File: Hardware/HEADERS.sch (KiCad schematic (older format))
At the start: 47 parts, among them J16 SPOX-3, J17 SPOX-3, J18 SPOX-4, J19 SPOX-2, J20 SPOX-3, J22 SPOX-4, J23 SPOX-4, J24 SPOX-6, J25 SPOX-6, J26 SPOX-6, J28 SPOX-6, J29 SPOX-6, J30 SPOX-6

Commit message: Add files via upload
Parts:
- removed TP19: GPIOL0_1_TST, Measurement_Points:Measurement_Point_Round-SMD-Pad_Small, symbol TEST
- removed TP22: GPIOL0_2_TST, Measurement_Points:Measurement_Point_Round-SMD-Pad_Small, symbol TEST
- removed TP30, TP31, TP32, TP33, TP34, TP35: TEST, Measurement_Points:Measurement_Point_Round-SMD-Pad_Small, symbol TEST
- added J21: SPOX-4, Connectors_Molex:Molex_SPOX-5267_22-03-5045_04x2.54mm_Straight, symbol SPOX-4
- added J27: SPOX-6, Connectors_Molex:Molex_SPOX-5267_22-03-5065_06x2.54mm_Straight, symbol SPOX-6
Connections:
- net GND: now also J21.1, J27.1
- net SCL1: now also J21.3
- net SDA1: now also J21.4
- net SPI1_CK: now also J27.5
- net SPI1_SDO: now also J27.4
- net SPI1_SI: now also J27.3
- net SPI1_SS: now also J27.2
- net V_I2C: now also J21.2
- net V_SPI: now also J27.6
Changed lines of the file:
@@
 DBG_TX_SAFETY
 $Comp
-L GND #PWR60
+L GND #PWR060
 U 1 1 5923E07E
 P 4050 5300
-F 0 "#PWR60" H 4050 5050 50  0001 C CNN
+F 0 "#PWR060" H 4050 5050 50  0001 C CNN
 F 1 "GND" H 4050 5150 50  0000 C CNN
 F 2 "" H 4050 5300 50  0001 C CNN
@@
 SCL4
 $Comp
-L GND #PWR61
+L GND #PWR061
 U 1 1 5923E229
 P 6500 5700
-F 0 "#PWR61" H 6500 5450 50  0001 C CNN
+F 0 "#PWR061" H 6500 5450 50  0001 C CNN
 F 1 "GND" H 6500 5550 50  0000 C CNN
 F 2 "" H 6500 5700 50  0001 C CNN
@@
 SPI5_CK
 $Comp
-L GND #PWR62
+L GND #PWR062
 U 1 1 5923EE9C
 P 9950 5850
-F 0 "#PWR62" H 9950 5600 50  0001 C CNN
+F 0 "#PWR062" H 9950 5600 50  0001 C CNN
 F 1 "GND" H 9950 5700 50  0000 C CNN
 F 2 "" H 9950 5850 50  0001 C CNN
@@
 $EndComp
 $Comp
-L GND #PWR58
+L GND #PWR063
 U 1 1 5923F1BC
 P 1600 5000
-F 0 "#PWR58" H 1600 4750 50  0001 C CNN
+F 0 "#PWR063" H 1600 4750 50  0001 C CNN
 F 1 "GND" H 1600 4850 50  0000 C CNN
 F 2 "" H 1600 5000 50  0001 C CNN
@@
 UHF_RX
 $Comp
-L GND #PWR59
+L GND #PWR064
 U 1 1 594AA8BD
 P 1900 7000
-F 0 "#PWR59" H 1900 6750 50  0001 C CNN
+F 0 "#PWR064" H 1900 6750 50  0001 C CNN
 F 1 "GND" H 1900 6850 50  0000 C CNN
 F 2 "" H 1900 7000 50  0001 C CNN
@@
 $EndComp
 $Comp
+L SPOX-6 J27
+U 1 1 595BDD44
+P 9000 2900
+F 0 "J27" H 9100 3250 60  0000 C CNN
+F 1 "SPOX-6" H 9100 2550 60  0000 C CNN
+F 2 "Connectors_Molex:Molex_SPOX-5267_22-03-5065_06x2.54mm_Straight" H 9000 3050 60  0001 C CNN
+F 3 "" H 9000 3050 60  0001 C CNN
+F 4 "CONN-005" H 9200 3350 60  0001 C CNN "part_num"
+	1    9000 2900
+	1    0    0    -1
+$EndComp
+$Comp
 L SPOX-6 J28
 U 1 1 595BDD92
@@
 $EndComp
 $Comp
+L SPOX-4 J21
+U 1 1 595C301B
+P 3700 3850
+F 0 "J21" H 3800 4100 60  0000 C CNN
+F 1 "SPOX-4" H 3800 3600 60  0000 C CNN
+F 2 "Connectors_Molex:Molex_SPOX-5267_22-03-5045_04x2.54mm_Straight" H 3700 3900 60  0001 C CNN
+F 3 "" H 3700 3900 60  0001 C CNN
+F 4 "CONN-003" H 3900 4200 60  0001 C CNN "part_num"
+	1    3700 3850
+	1    0    0    -1
+$EndComp
+$Comp
 L SPOX-4 J22
 U 1 1 595C306F
@@
 	1750 3800 1500 3800
 Wire Wire Line
-	4050 4600 4050 5300
+	3900 4000 4050 4000
+Wire Wire Line
+	4050 4000 4050 5300
 Wire Wire Line
 	4050 5150 3900 5150
 Wire Wire Line
 	3900 4600 4050 4600
+Connection ~ 4050 4600
 Connection ~ 4050 5150
 Wire Wire Line
@@
 	3900 4500 4200 4500
 Connection ~ 4200 4500
+Connection ~ 4200 3900
 Wire Wire Line
 	3900 3700 4500 3700
@@
 Wire Wire Line
 	3900 4950 4500 4950
+Wire Wire Line
+	3900 3900 4200 3900
 Wire Wire Line
 	5600 2900 6500 2900
@@
 	9300 3050 9200 3050
 Wire Wire Line
-	9850 2650 10100 2650
+	9200 2650 10100 2650
 Wire Wire Line
 	10100 3500 10100 4300
 Wire Wire Line
-	9950 4000 9950 5850
+	9200 3150 9950 3150
+Wire Wire Line
+	9950 3150 9950 5850
 Wire Wire Line
 	9850 2550 9850 2650
+Connection ~ 9850 2650
 Connection ~ 10100 3500
 Connection ~ 10100 4300
@@
 Wire Wire Line
 	9200 4000 9950 4000
+Connection ~ 9950 4000
 Wire Wire Line
 	3350 3500 3350 3600
@@
 $EndComp
 $Comp
-L TEST TP19
-U 1 1 5B2C6951
-P 3550 6150
-F 0 "TP19" V 3600 7000 50  0000 C BNN
-F 1 "GPIOL0_1_TST" V 3550 6650 50  0000 C CNN
-F 2 "Measurement_Points:Measurement_Point_Round-SMD-Pad_Small" H 3550 6150 50  0001 C CNN
-F 3 "" H 3550 6150 50  0001 C CNN
-	1    3550 6150
-	0    -1   -1   0
-$EndComp
-$Comp
 L TEST TP20
 U 1 1 5B2C6D6F
@@
 $EndComp
 $Comp
-L TEST TP22
-U 1 1 5B2C6D7B
-P 3550 6600
-F 0 "TP22" V 3600 7450 50  0000 C BNN
-F 1 "GPIOL0_2_TST" V 3550 7100 50  0000 C CNN
-F 2 "Measurement_Points:Measurement_Point_Round-SMD-Pad_Small" H 3550 6600 50  0001 C CNN
-F 3 "" H 3550 6600 50  0001 C CNN
-	1    3550 6600
-	0    -1   -1   0
-$EndComp
-$Comp
 L TEST TP23
 U 1 1 5B2C6F3D
@@
 Text HLabel 3550 6050 2    60   Input ~ 0
 TMS1_TST
-Text HLabel 3550 6150 2    60   Input ~ 0
-GPIOL0_1_TST
 Text HLabel 3550 6400 2    60   Input ~ 0
 TDO2_TST
 Text HLabel 3550 6500 2    60   Input ~ 0
 TMS2_TST
-Text HLabel 3550 6600 2    60   Input ~ 0
-GPIOL0_2_TST
 Text HLabel 3550 6850 2    60   Input ~ 0
 UART1_RTS_TST
@@
 Text HLabel 3550 7300 2    60   Input ~ 0
 UART2_CTS_TST
-$Comp
-L TEST TP32
-U 1 1 5B3C0C72
-P 9200 2750
-F 0 "TP32" H 9200 3050 50  0000 C BNN
-F 1 "TEST" H 9200 3000 50  0000 C CNN
-F 2 "Measurement_Points:Measurement_Point_Round-SMD-Pad_Small" H 9200 2750 50  0001 C CNN
-F 3 "" H 9200 2750 50  0001 C CNN
-	1    9200 2750
-	0    -1   -1   0
-$EndComp
-$Comp
-L TEST TP33
-U 1 1 5B3C0F1B
-P 9200 2850
-F 0 "TP33" H 9200 3150 50  0000 C BNN
-F 1 "TEST" H 9200 3100 50  0000 C CNN
-F 2 "Measurement_Points:Measurement_Point_Round-SMD-Pad_Small" H 9200 2850 50  0001 C CNN
-F 3 "" H 9200 2850 50  0001 C CNN
-	1    9200 2850
-	0    -1   -1   0
-$EndComp
-$Comp
-L TEST TP34
-U 1 1 5B3C1148
-P 9200 2950
-F 0 "TP34" H 9200 3250 50  0000 C BNN
-F 1 "TEST" H 9200 3200 50  0000 C CNN
-F 2 "Measurement_Points:Measurement_Point_Round-SMD-Pad_Small" H 9200 2950 50  0001 C CNN
-F 3 "" H 9200 2950 50  0001 C CNN
-	1    9200 2950
-	0    -1   -1   0
-$EndComp
-$Comp
-L TEST TP35
-U 1 1 5B3C1282
-P 9200 3050
-F 0 "TP35" H 9200 3350 50  0000 C BNN
-F 1 "TEST" H 9200 3300 50  0000 C CNN
-F 2 "Measurement_Points:Measurement_Point_Round-SMD-Pad_Small" H 9200 3050 50  0001 C CNN
-F 3 "" H 9200 3050 50  0001 C CNN
-	1    9200 3050
-	0    -1   -1   0
-$EndComp
-$Comp
-L TEST TP30
-U 1 1 5B3C1DA0
-P 3900 3700
-F 0 "TP30" H 3900 4000 50  0000 C BNN
-F 1 "TEST" H 3900 3950 50  0000 C CNN
-F 2 "Measurement_Points:Measurement_Point_Round-SMD-Pad_Small" H 3900 3700 50  0001 C CNN
-F 3 "" H 3900 3700 50  0001 C CNN
-	1    3900 3700
-	0    -1   -1   0
-$EndComp
-$Comp
-L TEST TP31
-U 1 1 5B3C21DB
-P 3900 3800
-F 0 "TP31" H 3900 4100 50  0000 C BNN
-F 1 "TEST" H 3900 4050 50  0000 C CNN
-F 2 "Measurement_Points:Measurement_Point_Round-SMD-Pad_Small" H 3900 3800 50  0001 C CNN
-F 3 "" H 3900 3800 50  0001 C CNN
-	1    3900 3800
-	0    -1   -1   0
-$EndComp
 $EndSCHEMATC

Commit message: Revert "Add files via upload"
This reverts commit 5604160992b0e2f63895336bcd07dee2b13465c5.
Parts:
- removed J21: SPOX-4, Connectors_Molex:Molex_SPOX-5267_22-03-5045_04x2.54mm_Straight, symbol SPOX-4
- removed J27: SPOX-6, Connectors_Molex:Molex_SPOX-5267_22-03-5065_06x2.54mm_Straight, symbol SPOX-6
- added TP19: GPIOL0_1_TST, Measurement_Points:Measurement_Point_Round-SMD-Pad_Small, symbol TEST
- added TP22: GPIOL0_2_TST, Measurement_Points:Measurement_Point_Round-SMD-Pad_Small, symbol TEST
- added TP30, TP31, TP32, TP33, TP34, TP35: TEST, Measurement_Points:Measurement_Point_Round-SMD-Pad_Small, symbol TEST
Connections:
- net SCL1: now also TP31.1
- net SDA1: now also TP30.1
- net SPI1_CK: now also TP32.1
- net SPI1_SDO: now also TP33.1
- net SPI1_SI: now also TP34.1
- net SPI1_SS: now also TP35.1
- new net GPIOL0_1_TST: TP19.1
- new net GPIOL0_2_TST: TP22.1
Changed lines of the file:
@@
 DBG_TX_SAFETY
 $Comp
-L GND #PWR060
+L GND #PWR60
 U 1 1 5923E07E
 P 4050 5300
-F 0 "#PWR060" H 4050 5050 50  0001 C CNN
+F 0 "#PWR60" H 4050 5050 50  0001 C CNN
 F 1 "GND" H 4050 5150 50  0000 C CNN
 F 2 "" H 4050 5300 50  0001 C CNN
@@
 SCL4
 $Comp
-L GND #PWR061
+L GND #PWR61
 U 1 1 5923E229
 P 6500 5700
-F 0 "#PWR061" H 6500 5450 50  0001 C CNN
+F 0 "#PWR61" H 6500 5450 50  0001 C CNN
 F 1 "GND" H 6500 5550 50  0000 C CNN
 F 2 "" H 6500 5700 50  0001 C CNN
@@
 SPI5_CK
 $Comp
-L GND #PWR062
+L GND #PWR62
 U 1 1 5923EE9C
 P 9950 5850
-F 0 "#PWR062" H 9950 5600 50  0001 C CNN
+F 0 "#PWR62" H 9950 5600 50  0001 C CNN
 F 1 "GND" H 9950 5700 50  0000 C CNN
 F 2 "" H 9950 5850 50  0001 C CNN
@@
 $EndComp
 $Comp
-L GND #PWR063
+L GND #PWR58
 U 1 1 5923F1BC
 P 1600 5000
-F 0 "#PWR063" H 1600 4750 50  0001 C CNN
+F 0 "#PWR58" H 1600 4750 50  0001 C CNN
 F 1 "GND" H 1600 4850 50  0000 C CNN
 F 2 "" H 1600 5000 50  0001 C CNN
@@
 UHF_RX
 $Comp
-L GND #PWR064
+L GND #PWR59
 U 1 1 594AA8BD
 P 1900 7000
-F 0 "#PWR064" H 1900 6750 50  0001 C CNN
+F 0 "#PWR59" H 1900 6750 50  0001 C CNN
 F 1 "GND" H 1900 6850 50  0000 C CNN
 F 2 "" H 1900 7000 50  0001 C CNN
@@
 $EndComp
 $Comp
-L SPOX-6 J27
-U 1 1 595BDD44
-P 9000 2900
-F 0 "J27" H 9100 3250 60  0000 C CNN
-F 1 "SPOX-6" H 9100 2550 60  0000 C CNN
-F 2 "Connectors_Molex:Molex_SPOX-5267_22-03-5065_06x2.54mm_Straight" H 9000 3050 60  0001 C CNN
-F 3 "" H 9000 3050 60  0001 C CNN
-F 4 "CONN-005" H 9200 3350 60  0001 C CNN "part_num"
-	1    9000 2900
-	1    0    0    -1
-$EndComp
-$Comp
 L SPOX-6 J28
 U 1 1 595BDD92
@@
 $EndComp
 $Comp
-L SPOX-4 J21
-U 1 1 595C301B
-P 3700 3850
-F 0 "J21" H 3800 4100 60  0000 C CNN
-F 1 "SPOX-4" H 3800 3600 60  0000 C CNN
-F 2 "Connectors_Molex:Molex_SPOX-5267_22-03-5045_04x2.54mm_Straight" H 3700 3900 60  0001 C CNN
-F 3 "" H 3700 3900 60  0001 C CNN
-F 4 "CONN-003" H 3900 4200 60  0001 C CNN "part_num"
-	1    3700 3850
-	1    0    0    -1
-$EndComp
-$Comp
 L SPOX-4 J22
 U 1 1 595C306F
@@
 	1750 3800 1500 3800
 Wire Wire Line
-	3900 4000 4050 4000
-Wire Wire Line
-	4050 4000 4050 5300
+	4050 4600 4050 5300
 Wire Wire Line
 	4050 5150 3900 5150
 Wire Wire Line
 	3900 4600 4050 4600
-Connection ~ 4050 4600
 Connection ~ 4050 5150
 Wire Wire Line
@@
 	3900 4500 4200 4500
 Connection ~ 4200 4500
-Connection ~ 4200 3900
 Wire Wire Line
 	3900 3700 4500 3700
@@
 Wire Wire Line
 	3900 4950 4500 4950
-Wire Wire Line
-	3900 3900 4200 3900
 Wire Wire Line
 	5600 2900 6500 2900
@@
 	9300 3050 9200 3050
 Wire Wire Line
-	9200 2650 10100 2650
+	9850 2650 10100 2650
 Wire Wire Line
 	10100 3500 10100 4300
 Wire Wire Line
-	9200 3150 9950 3150
-Wire Wire Line
-	9950 3150 9950 5850
+	9950 4000 9950 5850
 Wire Wire Line
 	9850 2550 9850 2650
-Connection ~ 9850 2650
 Connection ~ 10100 3500
 Connection ~ 10100 4300
@@
 Wire Wire Line
 	9200 4000 9950 4000
-Connection ~ 9950 4000
 Wire Wire Line
 	3350 3500 3350 3600
@@
 $EndComp
 $Comp
+L TEST TP19
+U 1 1 5B2C6951
+P 3550 6150
+F 0 "TP19" V 3600 7000 50  0000 C BNN
+F 1 "GPIOL0_1_TST" V 3550 6650 50  0000 C CNN
+F 2 "Measurement_Points:Measurement_Point_Round-SMD-Pad_Small" H 3550 6150 50  0001 C CNN
+F 3 "" H 3550 6150 50  0001 C CNN
+	1    3550 6150
+	0    -1   -1   0
+$EndComp
+$Comp
 L TEST TP20
 U 1 1 5B2C6D6F
@@
 $EndComp
 $Comp
+L TEST TP22
+U 1 1 5B2C6D7B
+P 3550 6600
+F 0 "TP22" V 3600 7450 50  0000 C BNN
+F 1 "GPIOL0_2_TST" V 3550 7100 50  0000 C CNN
+F 2 "Measurement_Points:Measurement_Point_Round-SMD-Pad_Small" H 3550 6600 50  0001 C CNN
+F 3 "" H 3550 6600 50  0001 C CNN
+	1    3550 6600
+	0    -1   -1   0
+$EndComp
+$Comp
 L TEST TP23
 U 1 1 5B2C6F3D
@@
 Text HLabel 3550 6050 2    60   Input ~ 0
 TMS1_TST
+Text HLabel 3550 6150 2    60   Input ~ 0
+GPIOL0_1_TST
 Text HLabel 3550 6400 2    60   Input ~ 0
 TDO2_TST
 Text HLabel 3550 6500 2    60   Input ~ 0
 TMS2_TST
+Text HLabel 3550 6600 2    60   Input ~ 0
+GPIOL0_2_TST
 Text HLabel 3550 6850 2    60   Input ~ 0
 UART1_RTS_TST
@@
 Text HLabel 3550 7300 2    60   Input ~ 0
 UART2_CTS_TST
+$Comp
+L TEST TP32
+U 1 1 5B3C0C72
+P 9200 2750
+F 0 "TP32" H 9200 3050 50  0000 C BNN
+F 1 "TEST" H 9200 3000 50  0000 C CNN
+F 2 "Measurement_Points:Measurement_Point_Round-SMD-Pad_Small" H 9200 2750 50  0001 C CNN
+F 3 "" H 9200 2750 50  0001 C CNN
+	1    9200 2750
+	0    -1   -1   0
+$EndComp
+$Comp
+L TEST TP33
+U 1 1 5B3C0F1B
+P 9200 2850
+F 0 "TP33" H 9200 3150 50  0000 C BNN
+F 1 "TEST" H 9200 3100 50  0000 C CNN
+F 2 "Measurement_Points:Measurement_Point_Round-SMD-Pad_Small" H 9200 2850 50  0001 C CNN
+F 3 "" H 9200 2850 50  0001 C CNN
+	1    9200 2850
+	0    -1   -1   0
+$EndComp
+$Comp
+L TEST TP34
+U 1 1 5B3C1148
+P 9200 2950
+F 0 "TP34" H 9200 3250 50  0000 C BNN
+F 1 "TEST" H 9200 3200 50  0000 C CNN
+F 2 "Measurement_Points:Measurement_Point_Round-SMD-Pad_Small" H 9200 2950 50  0001 C CNN
+F 3 "" H 9200 2950 50  0001 C CNN
+	1    9200 2950
+	0    -1   -1   0
+$EndComp
+$Comp
+L TEST TP35
+U 1 1 5B3C1282
+P 9200 3050
+F 0 "TP35" H 9200 3350 50  0000 C BNN
+F 1 "TEST" H 9200 3300 50  0000 C CNN
+F 2 "Measurement_Points:Measurement_Point_Round-SMD-Pad_Small" H 9200 3050 50  0001 C CNN
+F 3 "" H 9200 3050 50  0001 C CNN
+	1    9200 3050
+	0    -1   -1   0
+$EndComp
+$Comp
+L TEST TP30
+U 1 1 5B3C1DA0
+P 3900 3700
+F 0 "TP30" H 3900 4000 50  0000 C BNN
+F 1 "TEST" H 3900 3950 50  0000 C CNN
+F 2 "Measurement_Points:Measurement_Point_Round-SMD-Pad_Small" H 3900 3700 50  0001 C CNN
+F 3 "" H 3900 3700 50  0001 C CNN
+	1    3900 3700
+	0    -1   -1   0
+$EndComp
+$Comp
+L TEST TP31
+U 1 1 5B3C21DB
+P 3900 3800
+F 0 "TP31" H 3900 4100 50  0000 C BNN
+F 1 "TEST" H 3900 4050 50  0000 C CNN
+F 2 "Measurement_Points:Measurement_Point_Round-SMD-Pad_Small" H 3900 3800 50  0001 C CNN
+F 3 "" H 3900 3800 50  0001 C CNN
+	1    3900 3800
+	0    -1   -1   0
+$EndComp
 $EndSCHEMATC

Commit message: Updated REV1 branch with changes from USB Interface Revision
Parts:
- removed TP19: GPIOL0_1_TST, Measurement_Points:Measurement_Point_Round-SMD-Pad_Small, symbol TEST
- removed TP22: GPIOL0_2_TST, Measurement_Points:Measurement_Point_Round-SMD-Pad_Small, symbol TEST
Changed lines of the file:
@@
-$EndComp
-$Comp
-L TEST TP19
-U 1 1 5B2C6951
-P 3550 6150
-F 0 "TP19" V 3600 7000 50  0000 C BNN
-F 1 "GPIOL0_1_TST" V 3550 6650 50  0000 C CNN
-F 2 "Measurement_Points:Measurement_Point_Round-SMD-Pad_Small" H 3550 6150 50  0001 C CNN
-F 3 "" H 3550 6150 50  0001 C CNN
-	1    3550 6150
-	0    -1   -1   0
 $EndComp
 $Comp
@@
 F 3 "" H 3550 6500 50  0001 C CNN
 	1    3550 6500
-	0    -1   -1   0
-$EndComp
-$Comp
-L TEST TP22
-U 1 1 5B2C6D7B
-P 3550 6600
-F 0 "TP22" V 3600 7450 50  0000 C BNN
-F 1 "GPIOL0_2_TST" V 3550 7100 50  0000 C CNN
-F 2 "Measurement_Points:Measurement_Point_Round-SMD-Pad_Small" H 3550 6600 50  0001 C CNN
-F 3 "" H 3550 6600 50  0001 C CNN
-	1    3550 6600
 	0    -1   -1   0
 $EndComp
@@
 Text HLabel 3550 6050 2    60   Input ~ 0
 TMS1_TST
-Text HLabel 3550 6150 2    60   Input ~ 0
-GPIOL0_1_TST
 Text HLabel 3550 6400 2    60   Input ~ 0
 TDO2_TST
 Text HLabel 3550 6500 2    60   Input ~ 0
 TMS2_TST
-Text HLabel 3550 6600 2    60   Input ~ 0
-GPIOL0_2_TST
 Text HLabel 3550 6850 2    60   Input ~ 0
 UART1_RTS_TST

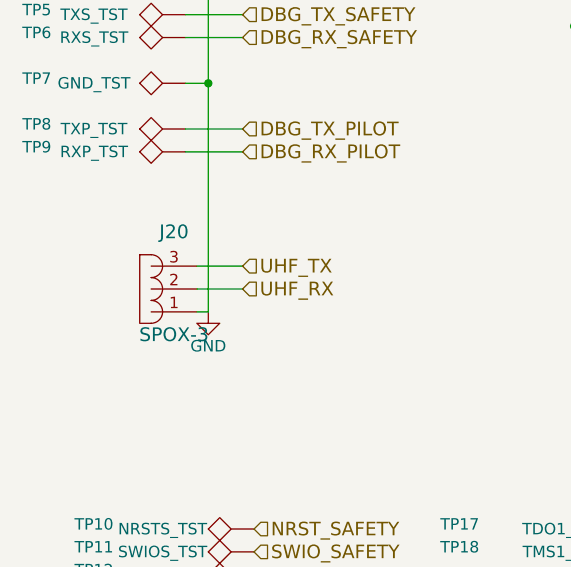
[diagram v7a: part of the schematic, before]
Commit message: Removed J20, added smaller inductor, updated placements
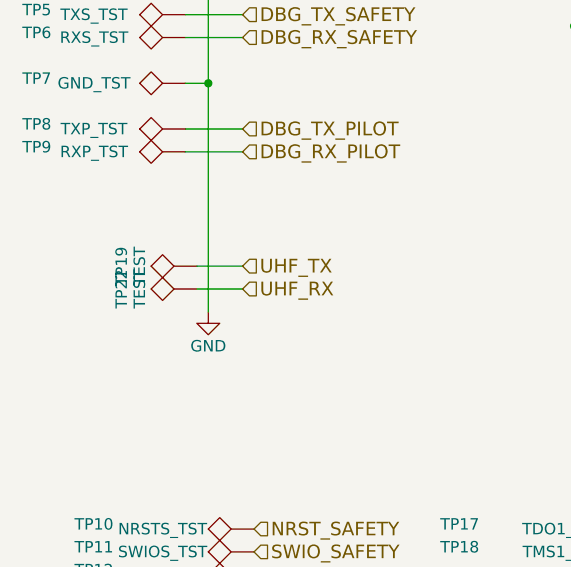
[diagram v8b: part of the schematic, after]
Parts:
- removed J20: SPOX-3, Connectors_Molex:Molex_SPOX-5267_22-03-5035_03x2.54mm_Straight, symbol SPOX-3
- added TP19, TP22: TEST, symbol TEST
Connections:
- net UHF_RX: now also TP22.1
- net UHF_TX: now also TP19.1
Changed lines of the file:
@@
 DBG_TX_SAFETY
 $Comp
-L GND #PWR60
+L GND #PWR060
 U 1 1 5923E07E
 P 4050 5300
-F 0 "#PWR60" H 4050 5050 50  0001 C CNN
+F 0 "#PWR060" H 4050 5050 50  0001 C CNN
 F 1 "GND" H 4050 5150 50  0000 C CNN
 F 2 "" H 4050 5300 50  0001 C CNN
@@
 SCL4
 $Comp
-L GND #PWR61
+L GND #PWR061
 U 1 1 5923E229
 P 6500 5700
-F 0 "#PWR61" H 6500 5450 50  0001 C CNN
+F 0 "#PWR061" H 6500 5450 50  0001 C CNN
 F 1 "GND" H 6500 5550 50  0000 C CNN
 F 2 "" H 6500 5700 50  0001 C CNN
@@
 SPI5_CK
 $Comp
-L GND #PWR62
+L GND #PWR062
 U 1 1 5923EE9C
 P 9950 5850
-F 0 "#PWR62" H 9950 5600 50  0001 C CNN
+F 0 "#PWR062" H 9950 5600 50  0001 C CNN
 F 1 "GND" H 9950 5700 50  0000 C CNN
 F 2 "" H 9950 5850 50  0001 C CNN
 F 3 "" H 9950 5850 50  0001 C CNN
 	1    9950 5850
-	1    0    0    -1
-$EndComp
-$Comp
-L GND #PWR58
-U 1 1 5923F1BC
-P 1600 5000
-F 0 "#PWR58" H 1600 4750 50  0001 C CNN
-F 1 "GND" H 1600 4850 50  0000 C CNN
-F 2 "" H 1600 5000 50  0001 C CNN
-F 3 "" H 1600 5000 50  0001 C CNN
-	1    1600 5000
 	1    0    0    -1
 $EndComp
@@
 UHF_RX
 $Comp
-L GND #PWR59
+L GND #PWR063
 U 1 1 594AA8BD
 P 1900 7000
-F 0 "#PWR59" H 1900 6750 50  0001 C CNN
+F 0 "#PWR063" H 1900 6750 50  0001 C CNN
 F 1 "GND" H 1900 6850 50  0000 C CNN
 F 2 "" H 1900 7000 50  0001 C CNN
@@
 $EndComp
 $Comp
-L SPOX-3 J20
-U 1 1 595BD8CE
-P 1350 4900
-F 0 "J20" H 1450 5150 60  0000 C CNN
-F 1 "SPOX-3" H 1450 4700 60  0000 C CNN
-F 2 "Connectors_Molex:Molex_SPOX-5267_22-03-5035_03x2.54mm_Straight" H 1350 5050 60  0001 C CNN
-F 3 "" H 1450 5150 60  0001 C CNN
-F 4 "CONN-002" H 1550 5250 60  0001 C CNN "part_num"
-	1    1350 4900
-	1    0    0    -1
-$EndComp
-$Comp
 L SPOX-6 J24
 U 1 1 595BDC13
@@
 Wire Wire Line
 	1750 4900 1550 4900
-Wire Wire Line
-	1600 5000 1550 5000
 Wire Wire Line
 	6600 2400 5600 2400
@@
 	0    -1   -1   0
 $EndComp
+$Comp
+L GND #PWR064
+U 1 1 5923F1BC
+P 1600 5000
+F 0 "#PWR064" H 1600 4750 50  0001 C CNN
+F 1 "GND" H 1600 4850 50  0000 C CNN
+F 2 "" H 1600 5000 50  0001 C CNN
+F 3 "" H 1600 5000 50  0001 C CNN
+	1    1600 5000
+	1    0    0    -1
+$EndComp
+$Comp
+L TEST TP19
+U 1 1 5B4E2465
+P 1550 4800
+F 0 "TP19" H 1550 5100 50  0000 C BNN
+F 1 "TEST" H 1550 5050 50  0000 C CNN
+F 2 "" H 1550 4800 50  0001 C CNN
+F 3 "" H 1550 4800 50  0001 C CNN
+	1    1550 4800
+	0    -1   -1   0
+$EndComp
+$Comp
+L TEST TP22
+U 1 1 5B4E251E
+P 1550 4900
+F 0 "TP22" H 1550 5200 50  0000 C BNN
+F 1 "TEST" H 1550 5150 50  0000 C CNN
+F 2 "" H 1550 4900 50  0001 C CNN
+F 3 "" H 1550 4900 50  0001 C CNN
+	1    1550 4900
+	0    -1   -1   0
+$EndComp
